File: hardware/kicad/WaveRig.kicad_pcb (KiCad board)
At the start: 2 copper layers, 0 parts

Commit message: fix: repair schematic connectivity, real MAX3421E pinout, footprint assignment
- Root sheet pins were placed outside the sheet boxes, so no cross-sheet
  net (IO5->CI-V, USB D+/D-, SPI, VBUS_5V, 5V_HOST) was actually connected.
  Rebuilt pins on the sheet borders with wire stubs + labels.
- MCU: SW1/SW2 pin 2 carried both GND and EN/BOOT0 (short to ground);
  GND moved to pin 1. Unused ESP32 GPIOs marked no-connect.
- USB_Host rebuilt around the real MAX3421E TQFN-32 pinout (datasheet
  19-3953): 33 ohm D+/D- series resistors, 1uF VCC/VBCOMP, 0.1uF VL.
- J1 now AudioJack3 (T/R/S) with CUI SJ1-3523N footprint; Q1 is a real
  2N7000 (TO-92).
- PWR_FLAGs added; ERC (raw kicad-cli) has 0 errors.
- Board outline 65x45 mm, 54 footprints assigned and written to symbol
  Footprint fields, netlist applied. Placement is a rough grid only; no
  routing yet.
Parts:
- added BT1: LiPo_3.7V_JST-PH, Connector_JST:JST_PH_B2B-PH-K_1x02_P2.00mm_Vertical, F.Cu at (13.0, 158.0)
- added C1: 100uF, Capacitor_SMD:C_1206_3216Metric, F.Cu at (20.5, 158.0)
- added C18: 100uF, Capacitor_SMD:C_1206_3216Metric, F.Cu at (28.0, 158.0)
- added C19: 22pF, Capacitor_SMD:C_0603_1608Metric, F.Cu at (35.5, 158.0)
- added C2: 100nF, Capacitor_SMD:C_0603_1608Metric, F.Cu at (43.0, 158.0)
- added C20: 22pF, Capacitor_SMD:C_0603_1608Metric, F.Cu at (50.5, 158.0)
- added C21: 1uF, Capacitor_SMD:C_0603_1608Metric, F.Cu at (58.0, 158.0)
- added C22: 100nF, Capacitor_SMD:C_0603_1608Metric, F.Cu at (43.0, 197.0)
- added C23: 1uF, Capacitor_SMD:C_0603_1608Metric, F.Cu at (50.5, 197.0)
- added C3: 10uF, Capacitor_SMD:C_0603_1608Metric, F.Cu at (65.5, 158.0)
- added C4: 100nF, Capacitor_SMD:C_0603_1608Metric, F.Cu at (13.0, 164.5)
- added C5: 100nF, Capacitor_SMD:C_0603_1608Metric, F.Cu at (20.5, 164.5)
- added C6: 100nF, Capacitor_SMD:C_0603_1608Metric, F.Cu at (28.0, 164.5)
- added C7: 100nF, Capacitor_SMD:C_0603_1608Metric, F.Cu at (35.5, 164.5)
- added C8: 100nF, Capacitor_SMD:C_0603_1608Metric, F.Cu at (43.0, 164.5)
- added CN1: OLED_SSD1306_I2C, Connector_JST:JST_PH_B4B-PH-K_1x04_P2.00mm_Vertical, F.Cu at (50.5, 164.5)
- added D1: SS34, Diode_SMD:D_SMA, F.Cu at (58.0, 164.5)
- added D2: P6SMB550CA, Diode_SMD:D_SMB, F.Cu at (65.5, 164.5)
- added D3: SS34, Diode_SMD:D_SMA, F.Cu at (13.0, 171.0)
- added D4: SMBJ5.0A_or_similar_TBD, Diode_SMD:D_SMB, F.Cu at (20.5, 171.0)
- added DSUB1: LD09S24A4GV00LF, Connector_Dsub:DSUB-9_Socket_Horizontal_P2.77x2.54mm_EdgePinOffset9.40mm, F.Cu at (28.0, 171.0)
- added J1: CIV_3.5mm_TRS_Jack, Connector_Audio:Jack_3.5mm_CUI_SJ1-3523N_Horizontal, F.Cu at (35.5, 171.0)
- added J2: USB-C_16P-F-SMT, Connector_USB:USB_C_Receptacle_GCT_USB4115-03-C, F.Cu at (43.0, 171.0)
- added J3: USB-A_Host, Connector_USB:USB_A_Receptacle_GCT_USB1046, F.Cu at (50.5, 171.0)
- added L1: 4.7uH, Inductor_SMD:L_6.3x6.3_H3, F.Cu at (58.0, 171.0)
- added L2: 4.7uH, Inductor_SMD:L_6.3x6.3_H3, F.Cu at (65.5, 171.0)
- added Q1: 2N7000, Package_TO_SOT_THT:TO-92_Inline, F.Cu at (13.0, 177.5)
- added Q2: FS8205A, Package_TO_SOT_SMD:SOT-23-6, F.Cu at (20.5, 177.5)
- added R1: 1.2k, Resistor_SMD:R_0603_1608Metric, F.Cu at (28.0, 177.5)
- added R10: 5.1k, Resistor_SMD:R_0603_1608Metric, F.Cu at (35.5, 177.5)
- added R11: TBD_calc_for_5V, Resistor_SMD:R_0603_1608Metric, F.Cu at (43.0, 177.5)
- added R12: TBD_calc_for_5V, Resistor_SMD:R_0603_1608Metric, F.Cu at (50.5, 177.5)
- added R13: 100k, Resistor_SMD:R_0603_1608Metric, F.Cu at (58.0, 177.5)
- added R14: 100k, Resistor_SMD:R_0603_1608Metric, F.Cu at (65.5, 177.5)
- added R15: 33R 1%, Resistor_SMD:R_0603_1608Metric, F.Cu at (28.0, 197.0)
- added R16: 33R 1%, Resistor_SMD:R_0603_1608Metric, F.Cu at (35.5, 197.0)
- added R2: 100k, Resistor_SMD:R_0603_1608Metric, F.Cu at (13.0, 184.0)
- added R3: 470k, Resistor_SMD:R_0603_1608Metric, F.Cu at (20.5, 184.0)
- added R4: 10k, Resistor_SMD:R_0603_1608Metric, F.Cu at (28.0, 184.0)
- added R5: 10k, Resistor_SMD:R_0603_1608Metric, F.Cu at (35.5, 184.0)
- added R6: 5.1k, Resistor_SMD:R_0603_1608Metric, F.Cu at (43.0, 184.0)
- added R7: 5.1k, Resistor_SMD:R_0603_1608Metric, F.Cu at (50.5, 184.0)
- added R8: 5.1k, Resistor_SMD:R_0603_1608Metric, F.Cu at (58.0, 184.0)
- added R9: 5.1k, Resistor_SMD:R_0603_1608Metric, F.Cu at (65.5, 184.0)
- added SW1: RESET, Button_Switch_SMD:SW_SPST_B3S-1000, F.Cu at (13.0, 190.5)
- added SW2: BOOT, Button_Switch_SMD:SW_SPST_B3S-1000, F.Cu at (20.5, 190.5)
- added U1: TC4056A, Package_SO:SOIC-8_3.9x4.9mm_P1.27mm, F.Cu at (28.0, 190.5)
- added U2: DW01A, Package_TO_SOT_SMD:SOT-23-6, F.Cu at (35.5, 190.5)
- added U3: MT3608, Package_TO_SOT_SMD:SOT-23-6, F.Cu at (43.0, 190.5)
- added U4: MAX202EESE+T, Package_SO:SOIC-16_4.55x10.3mm_P1.27mm, F.Cu at (50.5, 190.5)
- added U6: ESP32-S3-WROOM-1-N16R8, RF_Module:ESP32-S3-WROOM-1, F.Cu at (58.0, 190.5)
- added U7: MAX3421EETJ+, Package_DFN_QFN:QFN-32-1EP_5x5mm_P0.5mm_EP3.7x3.7mm, F.Cu at (65.5, 190.5)
- added U9: MT3608, Package_TO_SOT_SMD:SOT-23-6, F.Cu at (13.0, 197.0)
- added Y1: 12MHz, Crystal:Crystal_SMD_HC49-SD, F.Cu at (20.5, 197.0)
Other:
- board outline added: 65 x 45 mm

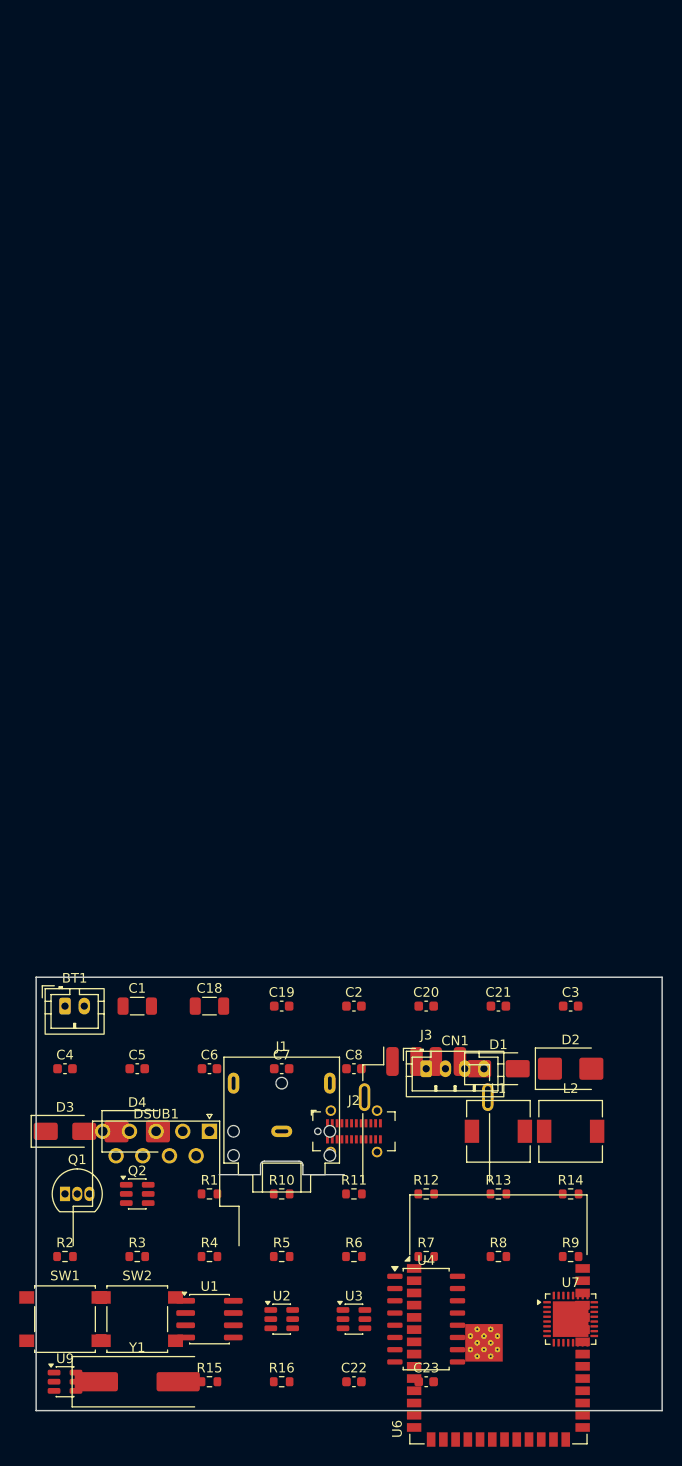
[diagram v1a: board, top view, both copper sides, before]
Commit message: fix: datasheet audit - correct charger pinout, LDO for 3V3, DW01A/FS8205A, MAX3232, CI-V RX
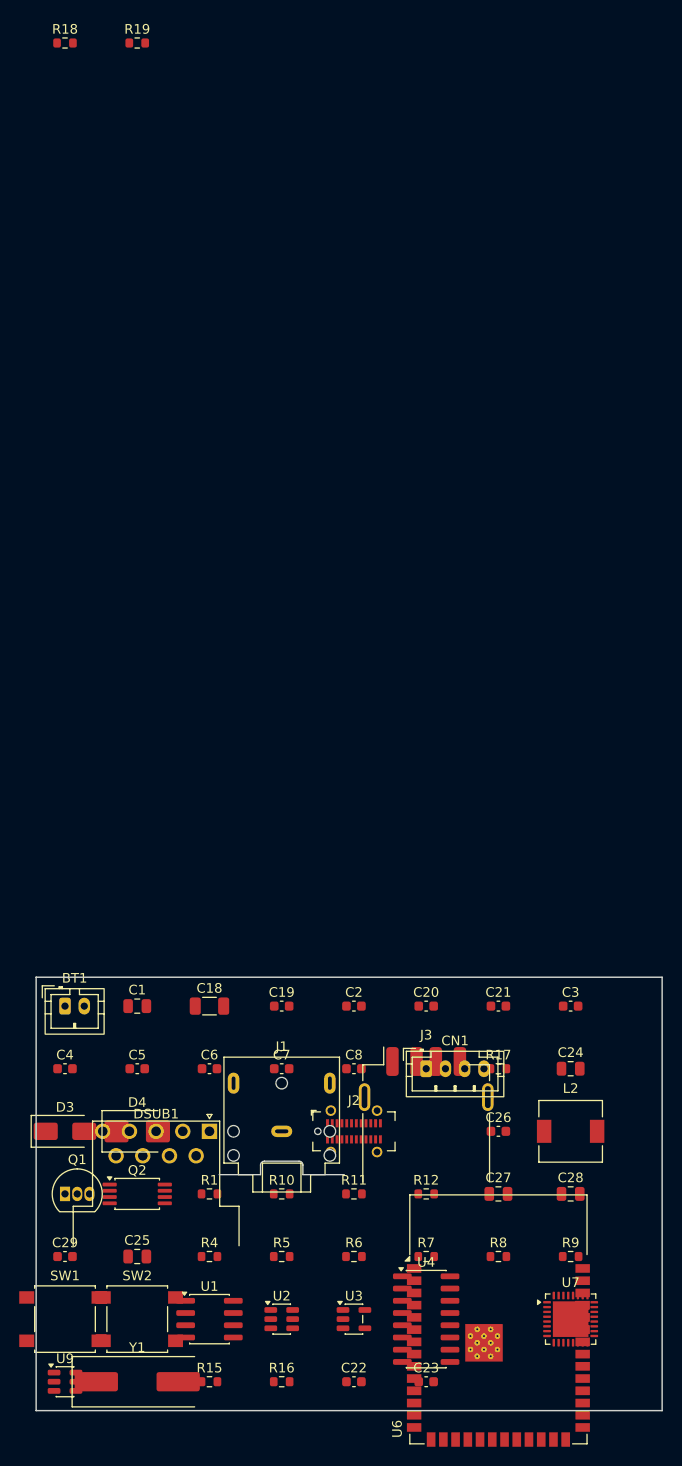
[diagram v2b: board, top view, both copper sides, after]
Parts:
- removed D1: SS34, Diode_SMD:D_SMA
- removed D2: P6SMB550CA, Diode_SMD:D_SMB
- removed L1: 4.7uH, Inductor_SMD:L_6.3x6.3_H3
- removed R13, R14, R2: 100k, Resistor_SMD:R_0603_1608Metric
- removed R3: 470k, Resistor_SMD:R_0603_1608Metric
- added C24: 10uF, Capacitor_SMD:C_0805_2012Metric, F.Cu at (65.5, 164.5)
- added C25: 10uF, Capacitor_SMD:C_0805_2012Metric, F.Cu at (20.5, 184.0)
- added C26: 100nF, Capacitor_SMD:C_0603_1608Metric, F.Cu at (58.0, 171.0)
- added C27: 10uF, Capacitor_SMD:C_0805_2012Metric, F.Cu at (58.0, 177.5)
- added C28: 10uF, Capacitor_SMD:C_0805_2012Metric, F.Cu at (65.5, 177.5)
- added C29: 1uF, Capacitor_SMD:C_0603_1608Metric, F.Cu at (13.0, 184.0)
- added R17: 100R, Resistor_SMD:R_0603_1608Metric, F.Cu at (58.0, 164.5)
- added R18: 1k, Resistor_SMD:R_0603_1608Metric, F.Cu at (13.0, 58.0)
- added R19: 4.7k, Resistor_SMD:R_0603_1608Metric, F.Cu at (20.5, 58.0)
- C1: value 100uF -> 22uF; footprint Capacitor_SMD:C_1206_3216Metric -> Capacitor_SMD:C_0805_2012Metric
- D4: value SMBJ5.0A_or_similar_TBD -> SMBJ5.0CA
- Q2: footprint Package_TO_SOT_SMD:SOT-23-6 -> Package_SO:TSSOP-8_4.4x3mm_P0.65mm
- R11: value TBD_calc_for_5V -> 732k 1%
- R12: value TBD_calc_for_5V -> 100k 1%
- U3: value MT3608 -> AP2112K-3.3; footprint Package_TO_SOT_SMD:SOT-23-6 -> Package_TO_SOT_SMD:SOT-23-5
- U4: value MAX202EESE+T -> MAX3232EESE+T; footprint Package_SO:SOIC-16_4.55x10.3mm_P1.27mm -> Package_SO:SOIC-16_3.9x9.9mm_P1.27mm
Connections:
- net Net-(Q1-D) renamed /CIV/CIV_TIP
- Q2 pad 1: /Power/BATT_MINUS_RAW -> unconnected-(Q2-D12-Pad1)
- Q2 pad 2: /Power/PROT_G1 -> /Power/BATT_MINUS_RAW
- Q2 pad 3: GND -> /Power/BATT_MINUS_RAW
- Q2 pad 4: /Power/PROT_G2 -> /Power/PROT_G1
- Q2 pad 5: unconnected-(Q2-D2-Pad5) -> /Power/PROT_G2
- Q2 pad 6: unconnected-(Q2-D1-Pad6) -> GND
- U1 pad 1: /Power/TEMP_SET -> GND
- U1 pad 3: unconnected-(U1-STDBY-Pad3) -> GND
- U1 pad 6: GND -> unconnected-(U1-~{STDBY}-Pad6)
- U2 pad 2: GND -> /Power/DW_CS
- U2 pad 5: /Power/BATT_PLUS -> /Power/DW_VCC
- U3 pad 1: /Power/SW1 -> /Power/BATT_PLUS
- U3 pad 3: /Power/FB1 -> /Power/BATT_PLUS
- U3 pad 4: /Power/BATT_PLUS -> unconnected-(U3-NC-Pad4)
- U3 pad 5: /Power/BATT_PLUS -> +3V3
- U6 pad 6: unconnected-(U6-IO6-Pad6) -> /CIV_RX

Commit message: docs: specify Y1 crystal parameters (CL18pF, ESR 60R max) per MAX3421E datasheet
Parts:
- Y1: value 12MHz -> 12MHz CL18pF ESR60R max
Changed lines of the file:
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@@
 			)
 		)
-		(property "Value" "12MHz"
+		(property "Value" "12MHz CL18pF ESR60R max"
 			(at 0 3.55 0)
 			(layer "F.Fab")
